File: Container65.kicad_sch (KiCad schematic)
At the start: 92 parts, among them J1 Conn_01x03, J2 Conn_01x06, J3 POGOm1, J4 POGOm2, J5 POGOf1, J6 POGOf2, U1 RP2040, U2 TYPE-C-31-M-12, U3 XC6206PxxxMR, U4 W25Q128JVS, U5 USB Boot, U6 Reset, U7 LEFT, U8 RIGHT, Y1 12MHz - 20pF

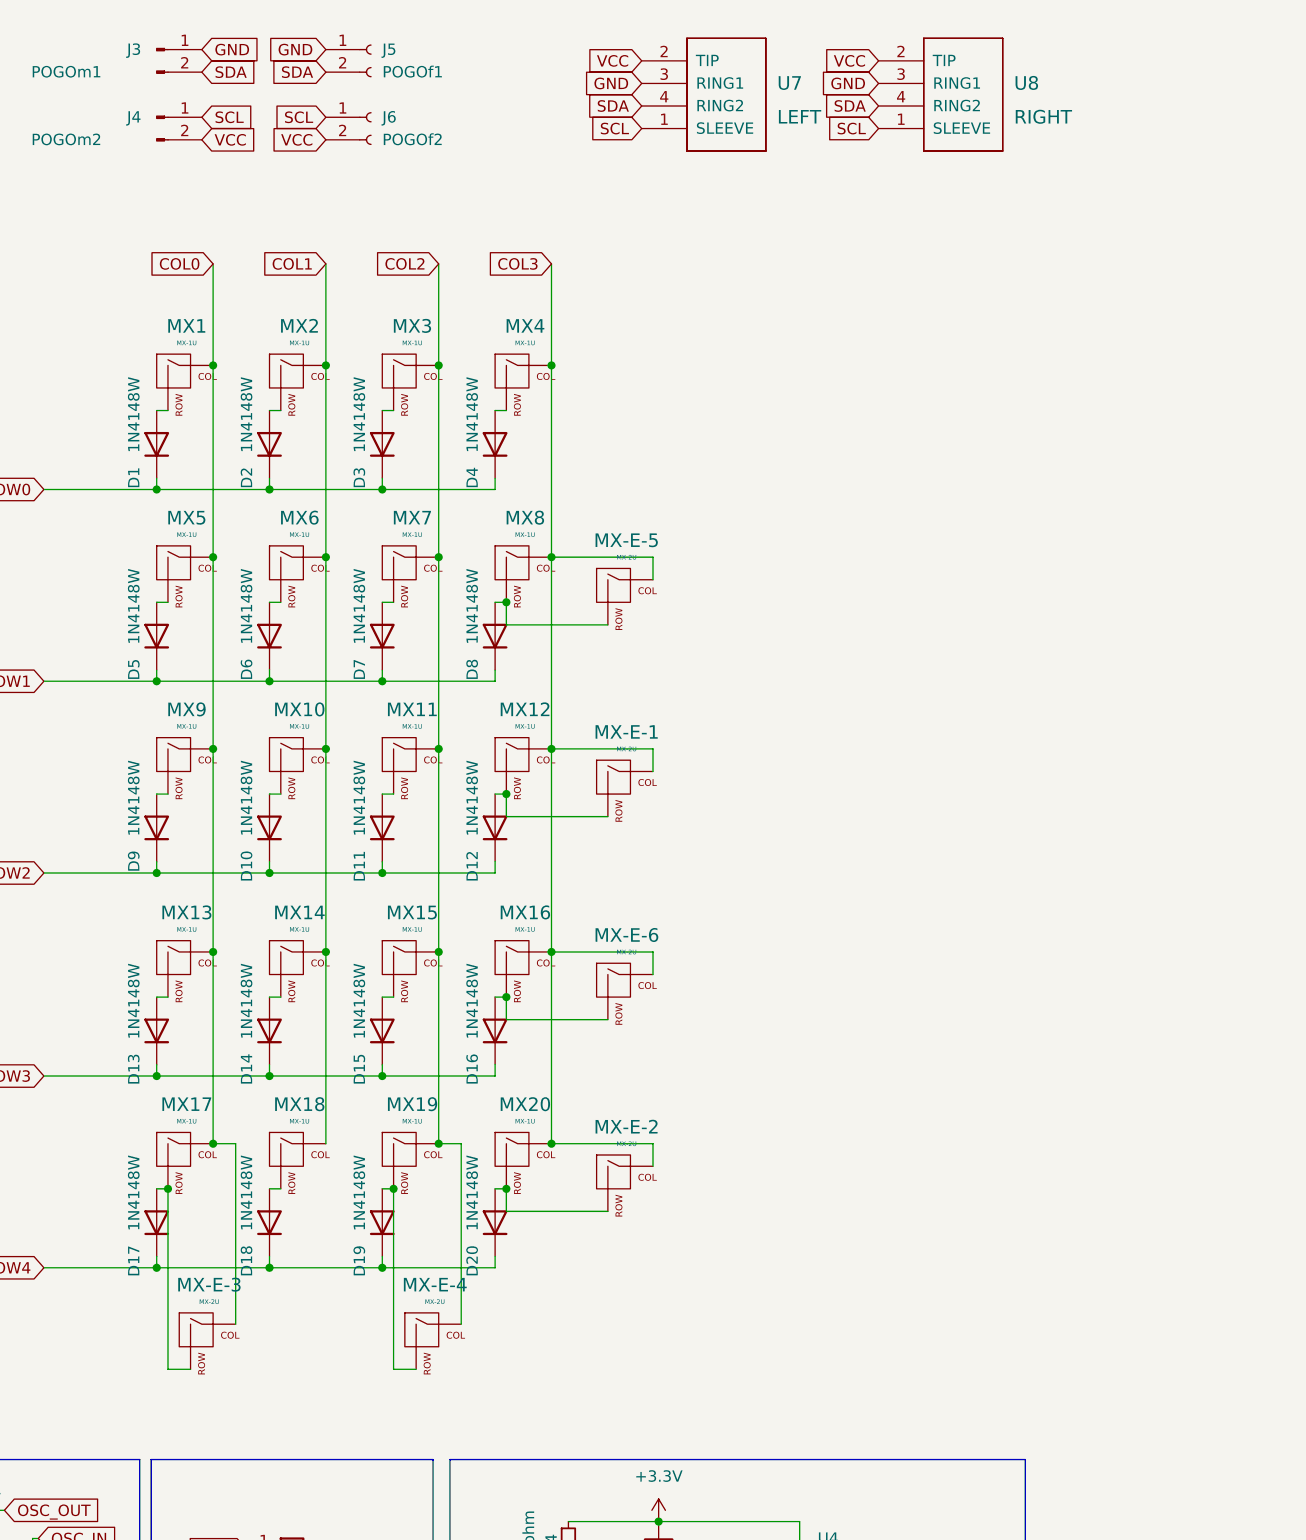
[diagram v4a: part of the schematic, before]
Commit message: Removed 1u
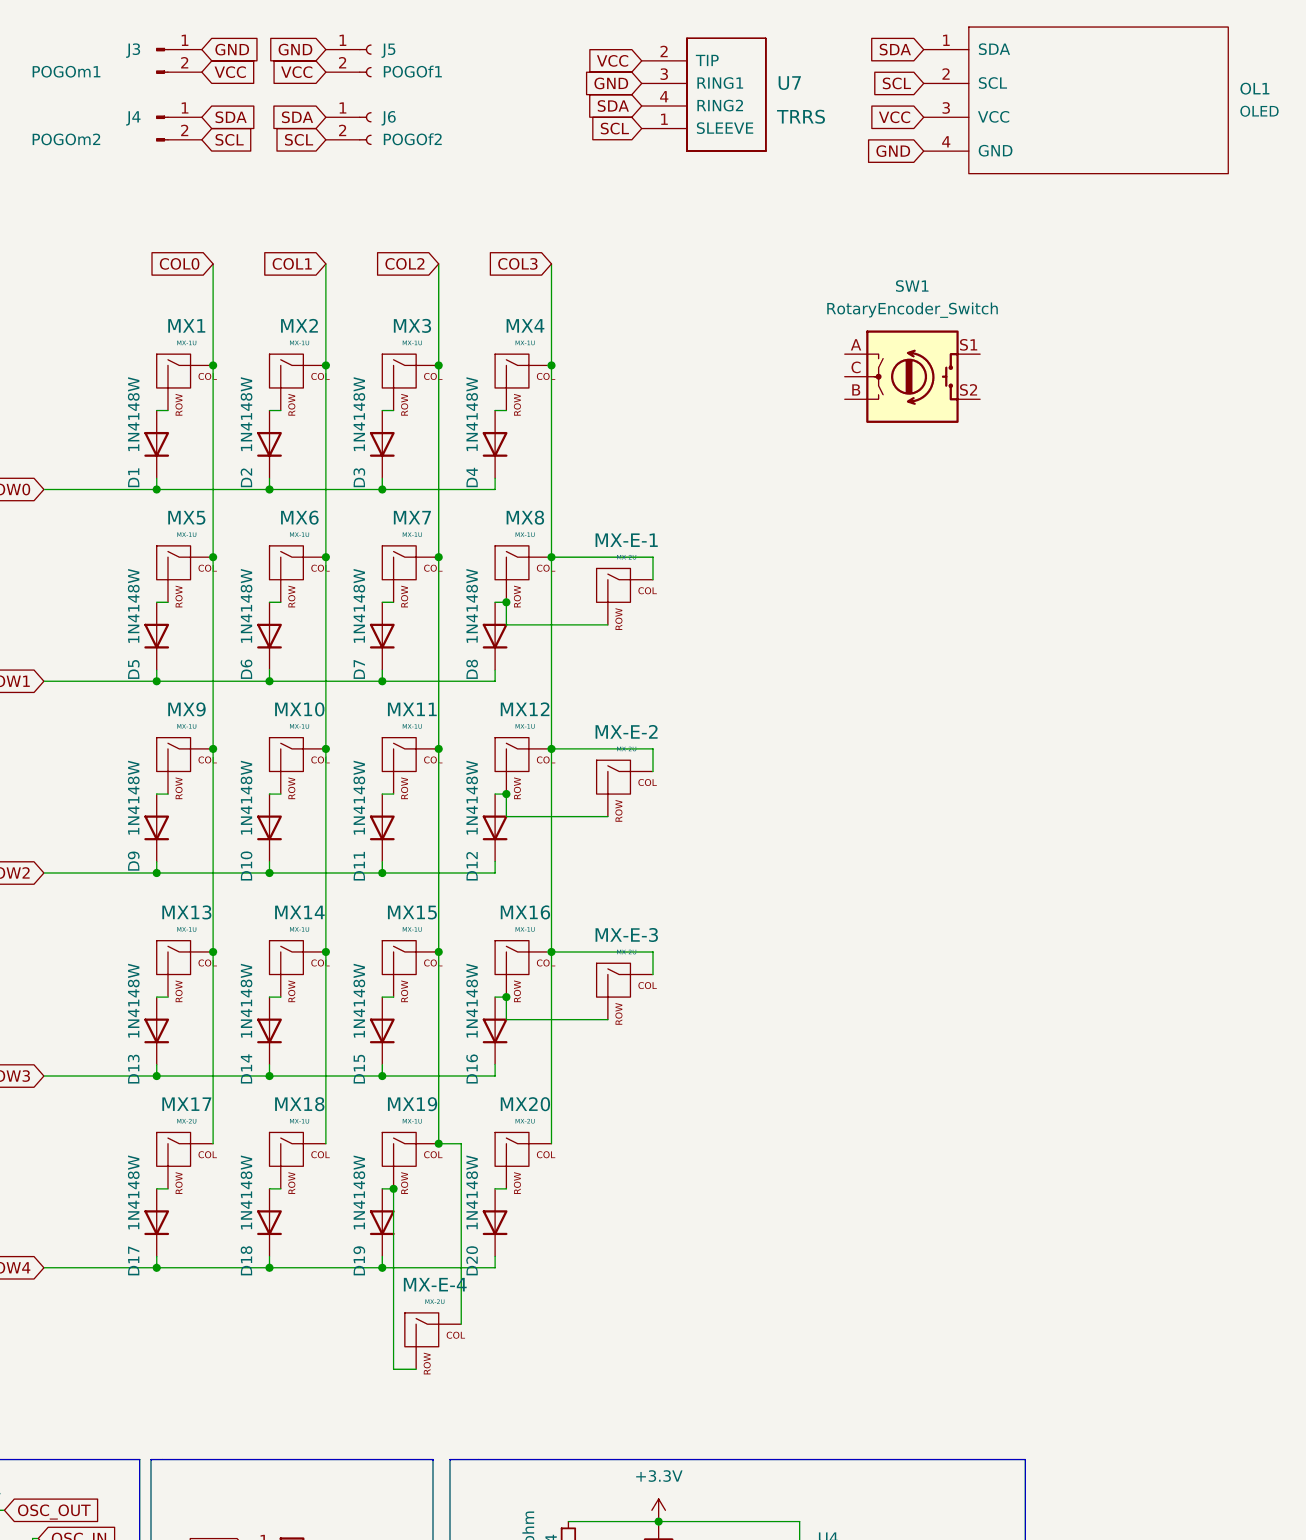
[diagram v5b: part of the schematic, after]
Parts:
- removed MX17, MX20: MX-1U, Switch_Keyboard_Hotswap_Kailh:SW_Hotswap_Kailh_MX_1.00u_Modified, symbol MX_Alps_Hybrid:MX-NoLED
- removed U8: RIGHT, Keebio-Parts:TRRS-PJ-320D, symbol keebio:TRRS
- added OL1: OLED, kbd:OLED_v2, symbol kbd:OLED
- added SW1: RotaryEncoder_Switch, Keebio-Parts:RotaryEncoder_EC11, symbol Device:RotaryEncoder_Switch
- U7: value LEFT -> TRRS; footprint Keebio-Parts:TRRS-PJ-320D -> Keebio-Parts:TRRS-PJ-320A
- renumbered MX-E-5 to MX-E-1, MX-E-1 to MX-E-2, MX-E-6 to MX-E-3, MX-E-3 to MX17, MX-E-2 to MX20
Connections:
- net GND: now also OL1.4 (GND)
- net SCL: now also J4.2 (Pin_2), J6.2 (Pin_2), OL1.2 (SCL); no longer J4.1 (Pin_1), J6.1 (Pin_1)
- net SDA: now also J4.1 (Pin_1), J6.1 (Pin_1), OL1.1 (SDA); no longer J3.2 (Pin_2), J5.2 (Pin_2)
- net VCC: now also J3.2 (Pin_2), J5.2 (Pin_2), OL1.3 (VCC); no longer J4.2 (Pin_2), J6.2 (Pin_2)
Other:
- moved on the sheet: MX17, MX20

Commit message: Finished routing MCU
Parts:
- removed J2: Conn_01x06, Connector_PinHeader_1.27mm:PinHeader_1x06_P1.27mm_Vertical, symbol Connector_Generic:Conn_01x06
- added D23: 1N4148W, Keebio-Parts:D_SOD123, symbol Diode:1N4148W
- added R10, R11: 4.7k, Keebio-Parts:R_0402, symbol Device:R_Small
- J3: footprint extras:1x02_2.54_Pogo Male GND -> Extras:1x02_2.54_Pogo Male GND
- J4: footprint extras:1x02_2.54_Pogo Male -> Extras:1x02_2.54_Pogo Male
- J5: footprint extras:1x02_2.54_Pogo Female GND -> Extras:1x02_2.54_Pogo Female GND
- J6: footprint extras:1x02_2.54_Pogo Female -> Extras:1x02_2.54_Pogo Female
- R1, R2: footprint Keebio-Parts:R_0402 -> Keebio-Parts:R_0603
- U1: footprint extras:rp2040 -> Extras:rp2040
- U2: footprint extras:simple-usb-c -> Extras:simple-usb-c
- U5, U6: footprint extras:tactile-switch -> Extras:3x4x2.5mm Micro Switch
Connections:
- net CLM5 is gone; now on net COL3: U1.13 (GPIO10)
- net CLM7 is gone; now on net ROW0: U1.14 (GPIO11)
- net VCC is gone; now on net +3V3: J3.2 (Pin_2), J5.2 (Pin_2), OL1.3 (VCC), U7.2 (TIP)
- net +3V3: now also R10.1, R11.1
- net COL3: now also SW1.S2
- net GND: now also SW1.C, U2.0
- net ROW0: now also D23.1 (K)
- net SCL: now also J4.1 (Pin_1), J6.1 (Pin_1), R11.2; no longer J4.2 (Pin_2), J6.2 (Pin_2)
- net SDA: now also J4.2 (Pin_2), J6.2 (Pin_2), R10.2; no longer J4.1 (Pin_1), J6.1 (Pin_1)
- net encB: now reaches SW1.A
- net encA: now reaches SW1.B
- net at SW1.S1: now also D23.2 (A)
- net CS: no longer names the net of U1.41 (GPIO29_ADC3)
- net MISO: no longer names the net of U1.40 (GPIO28_ADC2)
- net MOSI: no longer names the net of U1.39 (GPIO27_ADC1)
- net SCK: no longer names the net of U1.38 (GPIO26_ADC0)
- no-connect marks 14 -> 16
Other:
- moved on the sheet: J3, J4, J5, J6, SW1

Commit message: Finished routing
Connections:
- net CLM11 is gone; now on net ROW4: U1.31 (GPIO20)
- net CLM12 is gone; now on net ROW1: U1.34 (GPIO22)
- net CLM13 is gone; now on net ROW0: U1.35 (GPIO23)
- net CLM3 is gone; now on net ROW2: U1.29 (GPIO18)
- net CLM6 is gone; now on net ROW3: U1.30 (GPIO19)
- net ROW5 is gone; now on net COL1: U1.36 (GPIO24)
- net COL0: now also MX-E-1.1 (COL), MX-E-3.1 (COL), U1.37 (GPIO25); no longer MX17.1 (COL)
- net COL1: now also MX17.1 (COL)
- net COL2: now also U1.32 (GPIO21); no longer MX-E-4.1 (COL)
- net COL3: now also MX-E-4.1 (COL); no longer MX-E-1.1 (COL), MX-E-3.1 (COL)
- net ROW0: no longer U1.14 (GPIO11)
- net ROW1: no longer U1.37 (GPIO25)
- net ROW4: no longer U1.18 (GPIO15)
- net SCL: now also J4.2 (Pin_2), J6.2 (Pin_2), R10.2; no longer J4.1 (Pin_1), J6.1 (Pin_1), R11.2
- net SDA: now also J4.1 (Pin_1), J6.1 (Pin_1), R11.2; no longer J4.2 (Pin_2), J6.2 (Pin_2), R10.2
- net encA: now also U1.8 (GPIO6)
- net encB: now also U1.9 (GPIO7)
- net at D20.2 (A), MX20.2 (ROW): now also MX-E-4.2 (ROW)
- net at D19.2 (A), MX19.2 (ROW): no longer MX-E-4.2 (ROW)
- net at D8.2 (A), MX8.2 (ROW): no longer MX-E-1.2 (ROW)
- net at D16.2 (A), MX16.2 (ROW): no longer MX-E-3.2 (ROW)
- net at D13.2 (A), MX13.2 (ROW): now also MX-E-3.2 (ROW)
- net at D5.2 (A), MX5.2 (ROW): now also MX-E-1.2 (ROW)
- net CLM1: no longer names the net of U1.27 (GPIO16)
- net CLM10: no longer names the net of U1.17 (GPIO14)
- net CLM2: no longer names the net of U1.28 (GPIO17)
- net CLM8: no longer names the net of U1.15 (GPIO12)
- net CLM9: no longer names the net of U1.16 (GPIO13)
- no-connect marks 16 -> 13
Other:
- moved on the sheet: MX-E-1, MX-E-3, MX-E-4

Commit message: More routing fix
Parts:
- added X1, X2, X3, X4: 2u Stabilizer, Mounting_Keyboard_Stabilizer:Stabilizer_Cherry_MX_2.00u, symbol Connector:Conn_01x01_Male
- MX-E-1, MX-E-2, MX-E-3, MX-E-4, MX17, MX20: footprint Switch_Keyboard_Hotswap_Kailh:SW_Hotswap_Kailh_MX_1.00u_Extras -> Switch_Keyboard_Hotswap_Kailh:SW_Hotswap_Kailh_MX_plated_2.00u_Modified
- MX1, MX10, MX11, MX12, MX13, MX14, MX15, MX16, MX18, MX19, MX2, MX3, MX4, MX5, MX6, MX7, MX8, MX9: footprint Switch_Keyboard_Hotswap_Kailh:SW_Hotswap_Kailh_MX_1.00u_Modified -> Switch_Keyboard_Hotswap_Kailh:SW_Hotswap_Kailh_MX_plated_1.00u_Modified
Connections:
- net COL2: now also MX19.2 (ROW); no longer MX19.1 (COL)
- net COL3: now also MX-E-4.2 (ROW), U1.18 (GPIO15); no longer MX-E-4.1 (COL), U1.13 (GPIO10)
- net ROW2: now also U1.31 (GPIO20); no longer U1.29 (GPIO18)
- net ROW4: now also U1.29 (GPIO18); no longer U1.31 (GPIO20)
- net at D20.2 (A), MX20.2 (ROW): now also MX-E-4.1 (COL); no longer MX-E-4.2 (ROW)
- net at D19.2 (A): now also MX19.1 (COL); no longer MX19.2 (ROW)
- net at D9.2 (A), MX9.2 (ROW): now also MX-E-1.2 (ROW)
- net at D5.2 (A), MX5.2 (ROW): no longer MX-E-1.2 (ROW)
- no-connect marks 13 -> 24
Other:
- moved on the sheet: MX-E-4, MX19
